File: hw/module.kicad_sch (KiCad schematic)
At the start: 34 parts

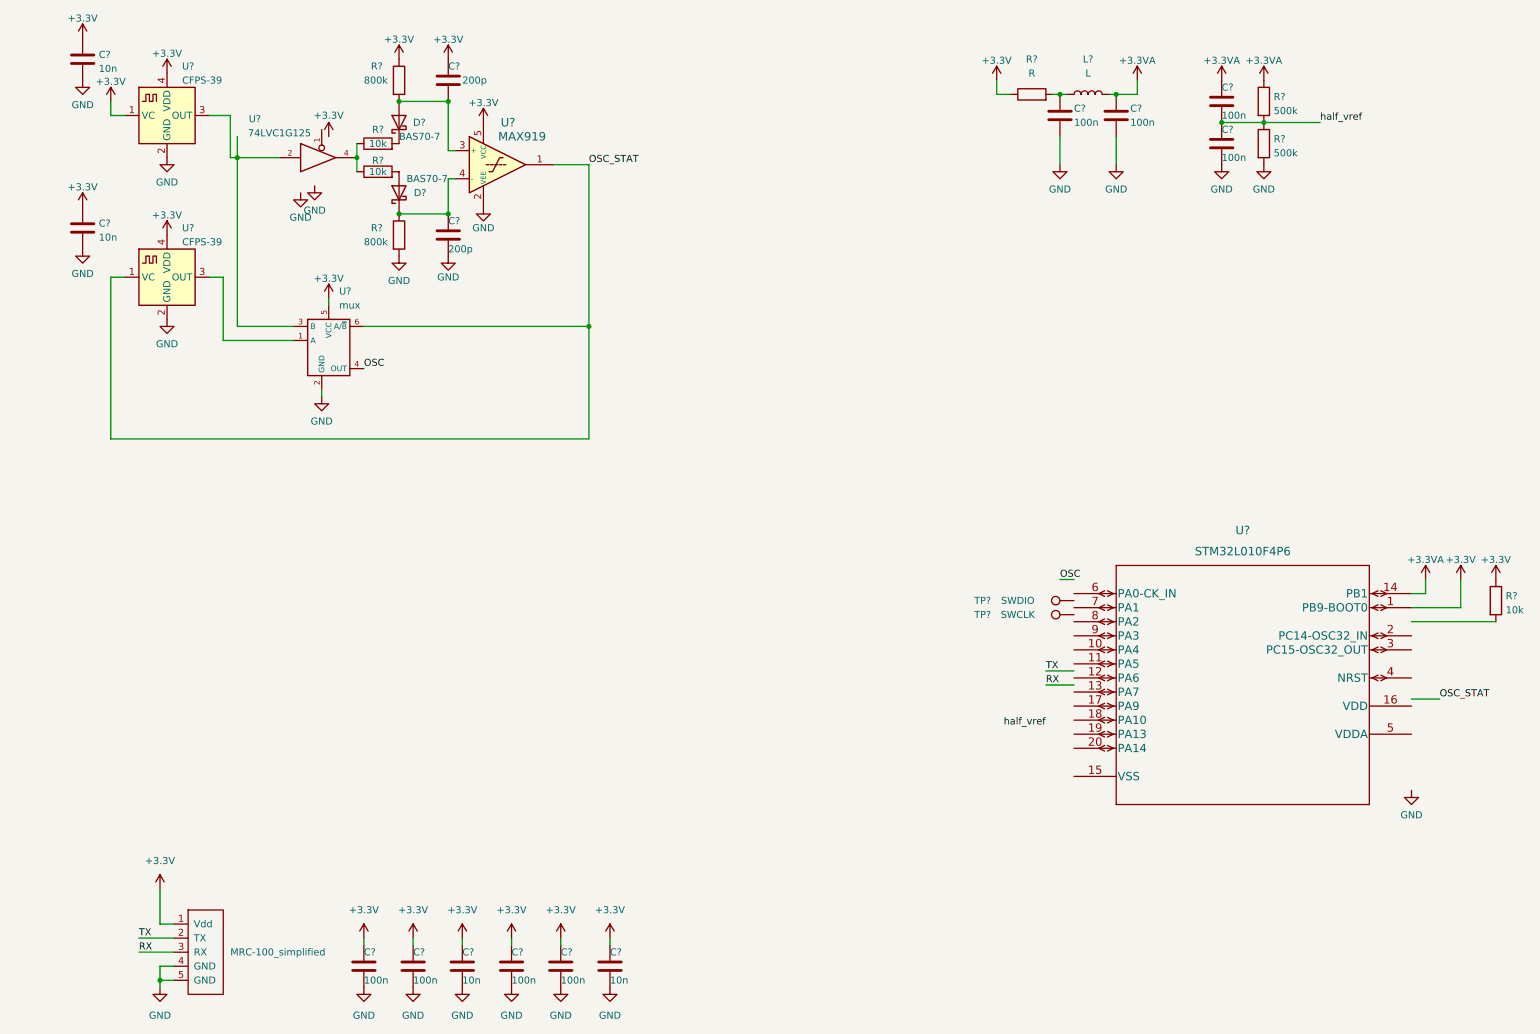
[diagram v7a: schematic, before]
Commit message: added bas70 symbol
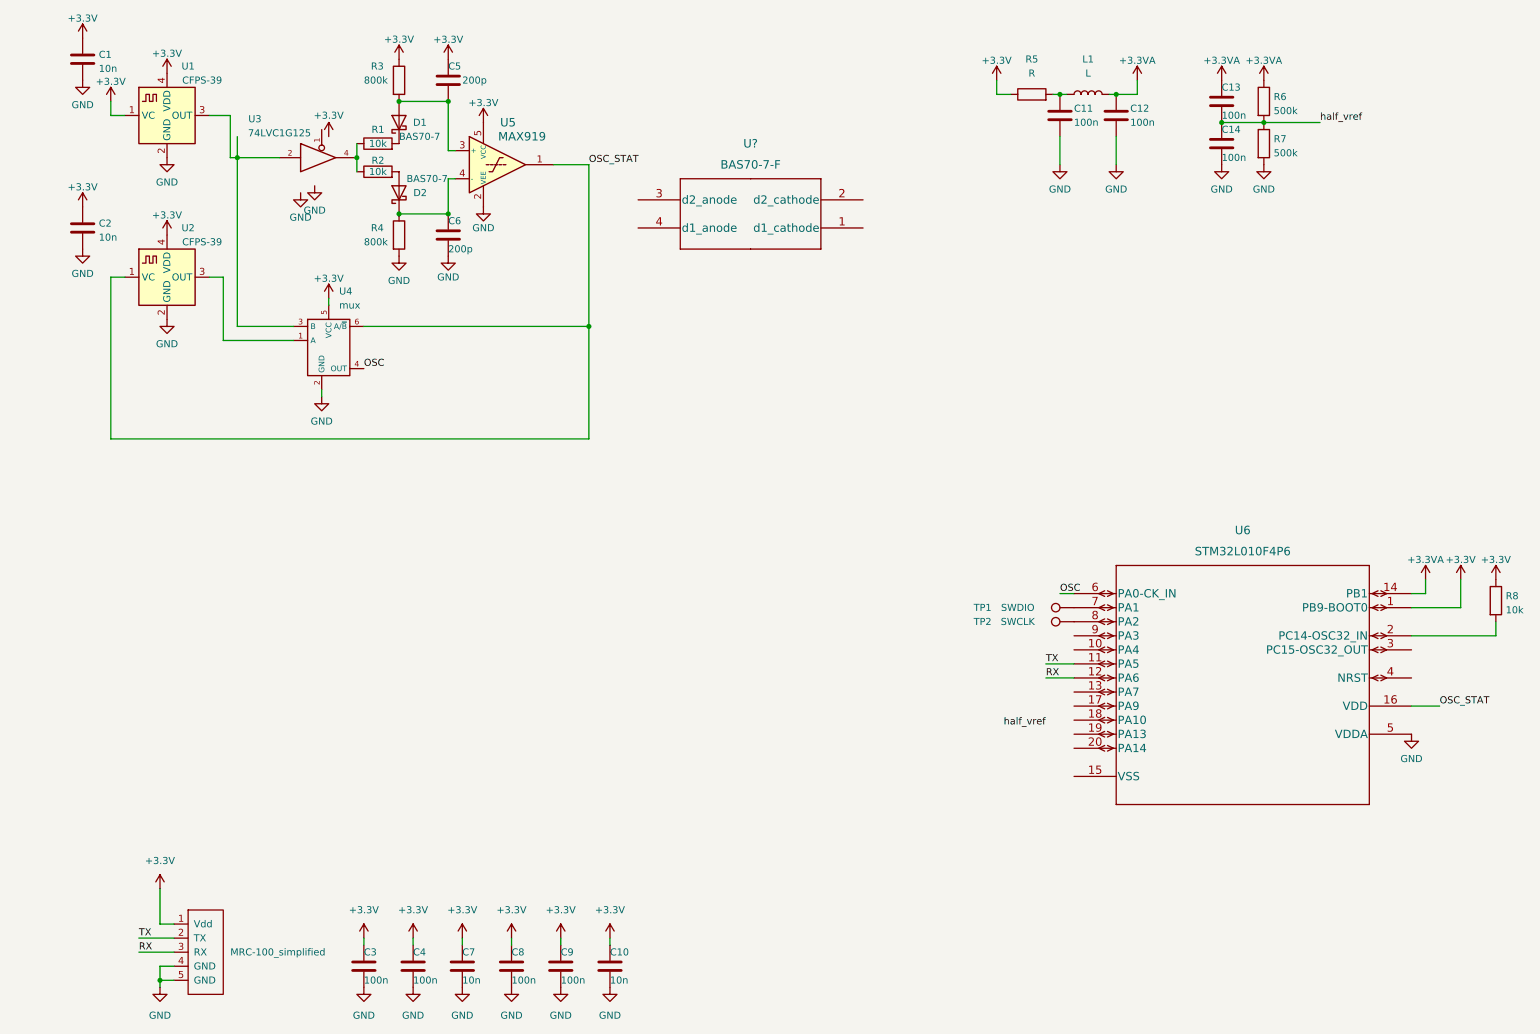
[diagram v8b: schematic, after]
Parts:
- added U?: BAS70-7-F, SOT-23_DIO, symbol bas70-7:BAS70-7-F
- C1, C10, C2, C3, C4, C5, C6, C7, C8, C9: renamed from C?; footprint Capacitor_SMD:C_0805_2012Metric_Pad1.18x1.45mm_HandSolder -> Capacitor_SMD:C_0201_0603Metric_Pad0.64x0.40mm_HandSolder
- L1: renamed from L?; footprint Inductor_SMD:L_0805_2012Metric_Pad1.15x1.40mm_HandSolder -> Inductor_SMD:L_0201_0603Metric_Pad0.64x0.40mm_HandSolder
- R1, R2, R3, R4, R5, R6, R7, R8: renamed from R?; footprint Resistor_SMD:R_0805_2012Metric_Pad1.20x1.40mm_HandSolder -> Resistor_SMD:R_0201_0603Metric_Pad0.64x0.40mm_HandSolder
- gave numbers to parts that had none: 14
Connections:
- net GND: now also U6.5 (VDDA)
- net OSC: now also U6.6 (PA0-CK_IN)
- net OSC_STAT: now also U6.16 (VDD)
- net RX: now also U6.12 (PA6)
- net TX: now also U6.11 (PA5)
- net at TP2.1: now also U6.8 (PA2)
- net at TP1.1: now also U6.7 (PA1)
- net at R8.2: now also U6.2 (PC14-OSC32_IN)
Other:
- moved on the sheet: TP1, TP2
